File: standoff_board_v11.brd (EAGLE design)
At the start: 27.6 x 34.3 mm, 20 parts

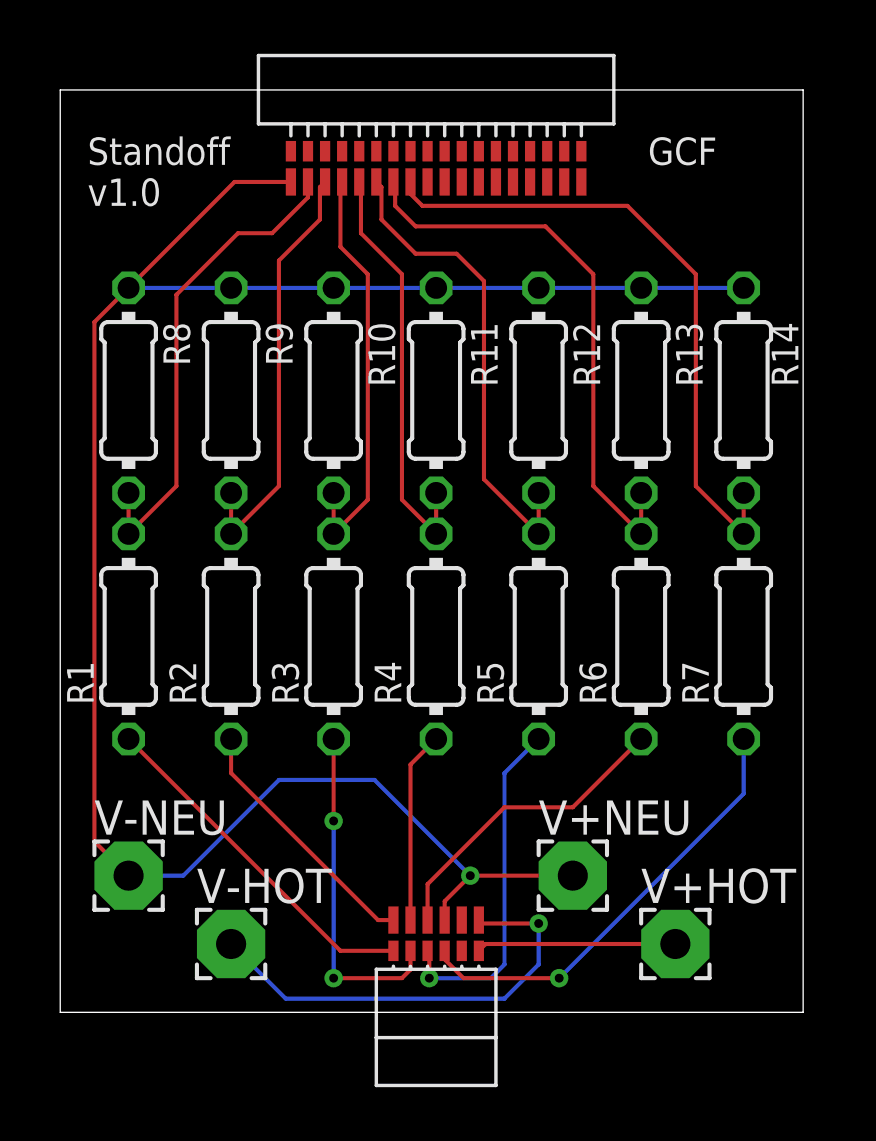
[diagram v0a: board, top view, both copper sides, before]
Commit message: Reroute output traces symmetrically
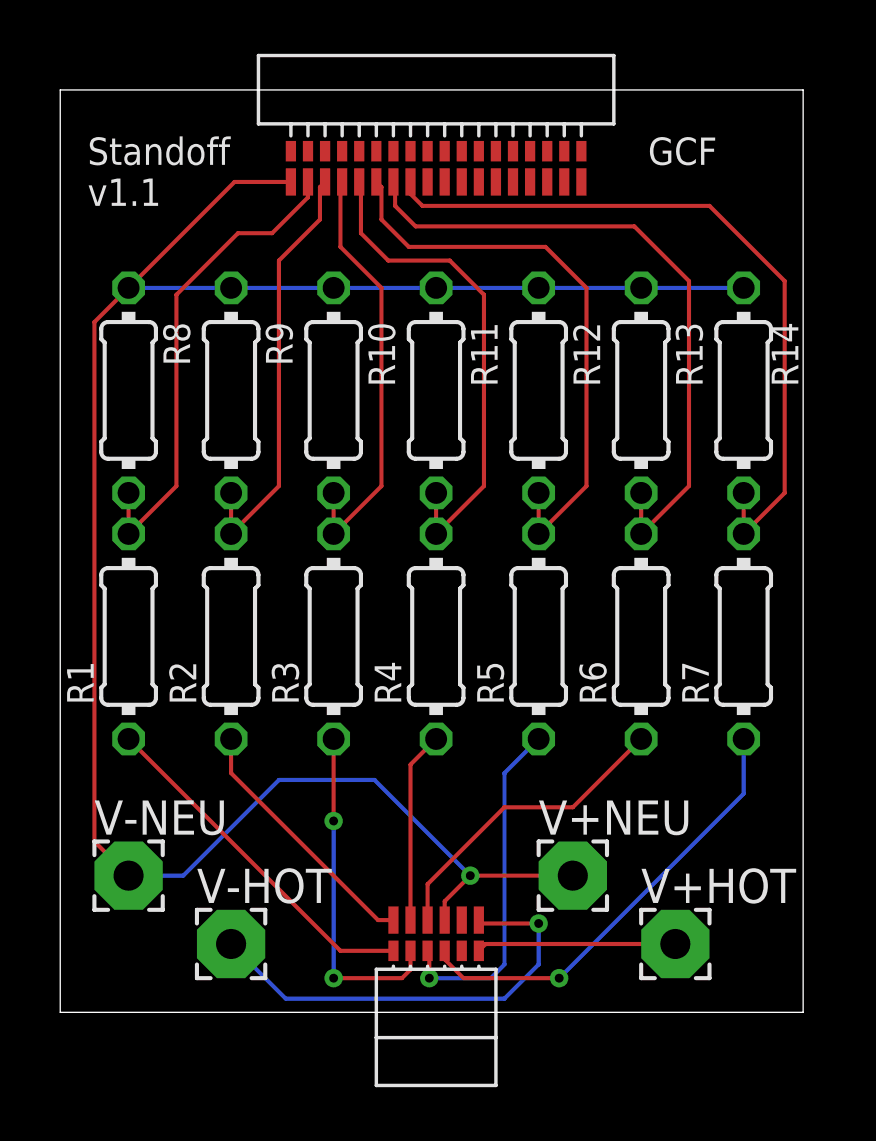
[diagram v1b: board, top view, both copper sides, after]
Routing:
- net A5POST: track 18.0 -> 21.6 mm
- net A6POST: track 21.2 -> 24.7 mm
- net A7POST: track 24.2 -> 27.2 mm
- net A4POST: track 15.8 -> 18.6 mm
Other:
- board text added: "Standoff v1.1"
- board text removed: "Standoff v1.0"
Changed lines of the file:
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@@
 <wire x1="0" y1="34.28" x2="0" y2="0" width="0" layer="20"/>
 <text x="1.016" y="29.972" size="1.016" layer="21" font="vector">Standoff
-v1.0</text>
+v1.1</text>
 <text x="21.844" y="31.496" size="1.016" layer="21" font="vector">GCF</text>
 </plain>
@@
 <contactref element="S2" pad="T4"/>
 <wire x1="10.16" y1="19.304" x2="10.16" y2="17.78" width="0.1524" layer="1"/>
-<wire x1="10.16" y1="17.78" x2="11.43" y2="19.05" width="0.1524" layer="1"/>
-<wire x1="11.43" y1="19.05" x2="11.43" y2="27.432" width="0.1524" layer="1"/>
-<wire x1="11.43" y1="27.432" x2="10.414" y2="28.448" width="0.1524" layer="1"/>
 <wire x1="10.414" y1="28.448" x2="10.414" y2="30.7975" width="0.1524" layer="1"/>
 <wire x1="10.414" y1="30.7975" x2="10.4775" y2="30.861" width="0.1524" layer="1"/>
+<wire x1="10.16" y1="17.78" x2="11.938" y2="19.558" width="0.1524" layer="1"/>
+<wire x1="11.938" y1="19.558" x2="11.938" y2="26.924" width="0.1524" layer="1"/>
+<wire x1="11.938" y1="26.924" x2="10.414" y2="28.448" width="0.1524" layer="1"/>
 </signal>
 <signal name="A4POST">
@@
 <contactref element="S2" pad="T5"/>
 <wire x1="13.97" y1="19.304" x2="13.97" y2="17.78" width="0.1524" layer="1"/>
-<wire x1="13.97" y1="17.78" x2="12.7" y2="19.05" width="0.1524" layer="1"/>
-<wire x1="12.7" y1="19.05" x2="12.7" y2="27.432" width="0.1524" layer="1"/>
-<wire x1="12.7" y1="27.432" x2="11.176" y2="28.956" width="0.1524" layer="1"/>
 <wire x1="11.176" y1="28.956" x2="11.176" y2="30.7975" width="0.1524" layer="1"/>
 <wire x1="11.176" y1="30.7975" x2="11.1125" y2="30.861" width="0.1524" layer="1"/>
+<wire x1="13.97" y1="17.78" x2="15.748" y2="19.558" width="0.1524" layer="1"/>
+<wire x1="15.748" y1="19.558" x2="15.748" y2="26.67" width="0.1524" layer="1"/>
+<wire x1="15.748" y1="26.67" x2="14.478" y2="27.94" width="0.1524" layer="1"/>
+<wire x1="14.478" y1="27.94" x2="12.192" y2="27.94" width="0.1524" layer="1"/>
+<wire x1="12.192" y1="27.94" x2="11.176" y2="28.956" width="0.1524" layer="1"/>
 </signal>
 <signal name="A5POST">
@@
 <contactref element="S2" pad="T6"/>
 <wire x1="17.78" y1="17.78" x2="17.78" y2="19.304" width="0.1524" layer="1"/>
-<wire x1="17.78" y1="17.78" x2="15.748" y2="19.812" width="0.1524" layer="1"/>
-<wire x1="13.208" y1="28.194" x2="11.938" y2="29.464" width="0.1524" layer="1"/>
 <wire x1="11.938" y1="29.464" x2="11.938" y2="30.6705" width="0.1524" layer="1"/>
 <wire x1="11.938" y1="30.6705" x2="11.7475" y2="30.861" width="0.1524" layer="1"/>
-<wire x1="13.208" y1="28.194" x2="14.732" y2="28.194" width="0.1524" layer="1"/>
-<wire x1="14.732" y1="28.194" x2="15.748" y2="27.178" width="0.1524" layer="1"/>
-<wire x1="15.748" y1="27.178" x2="15.748" y2="19.812" width="0.1524" layer="1"/>
+<wire x1="17.78" y1="17.78" x2="19.558" y2="19.558" width="0.1524" layer="1"/>
+<wire x1="19.558" y1="19.558" x2="19.558" y2="26.924" width="0.1524" layer="1"/>
+<wire x1="19.558" y1="26.924" x2="18.034" y2="28.448" width="0.1524" layer="1"/>
+<wire x1="18.034" y1="28.448" x2="12.954" y2="28.448" width="0.1524" layer="1"/>
+<wire x1="12.954" y1="28.448" x2="11.938" y2="29.464" width="0.1524" layer="1"/>
 </signal>
 <signal name="A6POST">
@@
 <contactref element="S2" pad="T7"/>
 <wire x1="21.59" y1="17.78" x2="21.59" y2="19.304" width="0.1524" layer="1"/>
-<wire x1="21.59" y1="17.78" x2="19.812" y2="19.558" width="0.1524" layer="1"/>
 <wire x1="13.208" y1="29.21" x2="12.446" y2="29.972" width="0.1524" layer="1"/>
 <wire x1="12.446" y1="29.972" x2="12.446" y2="30.7975" width="0.1524" layer="1"/>
 <wire x1="12.446" y1="30.7975" x2="12.3825" y2="30.861" width="0.1524" layer="1"/>
-<wire x1="19.812" y1="19.558" x2="19.812" y2="27.432" width="0.1524" layer="1"/>
-<wire x1="19.812" y1="27.432" x2="18.034" y2="29.21" width="0.1524" layer="1"/>
-<wire x1="18.034" y1="29.21" x2="13.208" y2="29.21" width="0.1524" layer="1"/>
+<wire x1="21.336" y1="29.21" x2="13.208" y2="29.21" width="0.1524" layer="1"/>
+<wire x1="21.59" y1="17.78" x2="23.368" y2="19.558" width="0.1524" layer="1"/>
+<wire x1="23.368" y1="19.558" x2="23.368" y2="27.178" width="0.1524" layer="1"/>
+<wire x1="23.368" y1="27.178" x2="21.336" y2="29.21" width="0.1524" layer="1"/>
 </signal>
 <signal name="A7POST">
@@
 <contactref element="S2" pad="T8"/>
 <wire x1="25.4" y1="17.78" x2="25.4" y2="19.304" width="0.1524" layer="1"/>
-<wire x1="25.4" y1="17.78" x2="23.622" y2="19.558" width="0.1524" layer="1"/>
 <wire x1="13.462" y1="29.972" x2="13.0175" y2="30.4165" width="0.1524" layer="1"/>
 <wire x1="13.0175" y1="30.4165" x2="13.0175" y2="30.861" width="0.1524" layer="1"/>
-<wire x1="23.622" y1="19.558" x2="23.622" y2="27.432" width="0.1524" layer="1"/>
-<wire x1="23.622" y1="27.432" x2="21.082" y2="29.972" width="0.1524" layer="1"/>
-<wire x1="21.082" y1="29.972" x2="13.462" y2="29.972" width="0.1524" layer="1"/>
+<wire x1="24.13" y1="29.972" x2="13.462" y2="29.972" width="0.1524" layer="1"/>
+<wire x1="25.4" y1="17.78" x2="26.924" y2="19.304" width="0.1524" layer="1"/>
+<wire x1="26.924" y1="19.304" x2="26.924" y2="27.178" width="0.1524" layer="1"/>
+<wire x1="26.924" y1="27.178" x2="24.13" y2="29.972" width="0.1524" layer="1"/>
 </signal>
 <signal name="GND">
